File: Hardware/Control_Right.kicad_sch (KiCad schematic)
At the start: 28 parts, among them J4 BAT, J5 TagConnect, J6 1.08_MIP_MODULE, Q2 AO3401A, SW3 MSK12C02, SW4 SW_Push, U3 TPS61040DBV, U4 XIAO-NRF52840-PLUS

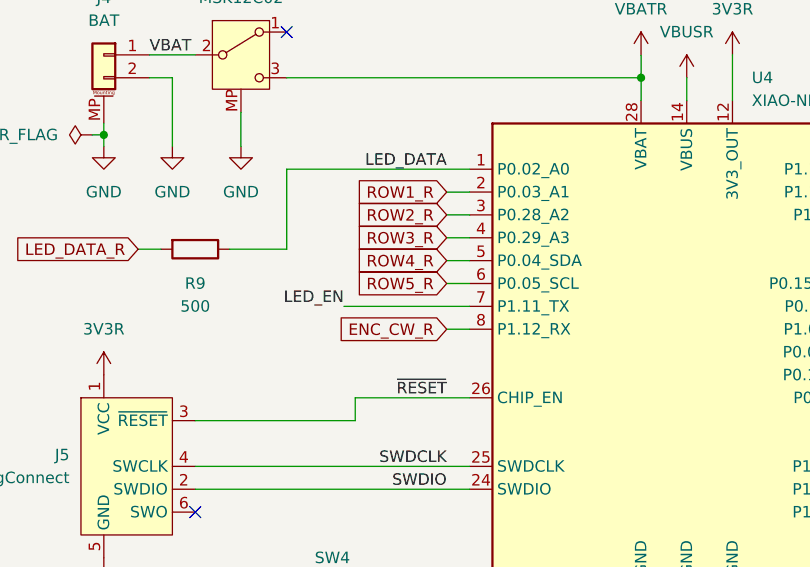
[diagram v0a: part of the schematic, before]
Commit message: Row removal and key layout
Removed the number row.
Adjusted the spacebar position and changed it to 1u.
Need to consider what to do for one of the halfs if its screen is to be removed.
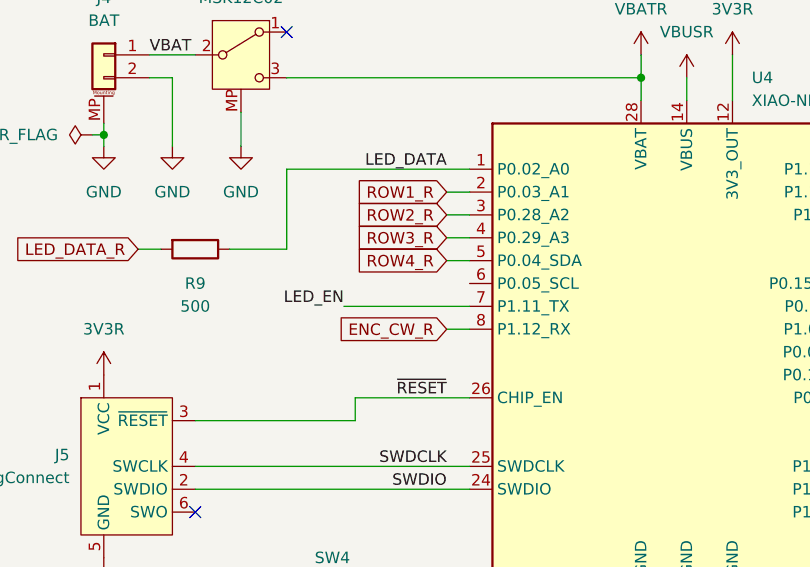
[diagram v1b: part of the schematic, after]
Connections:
- net ROW5_R: no longer names the net of U4.6 (P0.05_SCL)
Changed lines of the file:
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@@
-	(wire
-		(pts
-			(xy 87.63 66.04) (xy 90.17 66.04)
-		)
-		(stroke
-			(width 0)
-			(type default)
-		)
-	)
 	(wire
 		(pts
@@
 			)
 		)
-	)
-	(global_label "ROW5_R"
-		(shape input)
-		(at 87.63 66.04 180)
-		(fields_autoplaced yes)
-		(effects
-			(font
-				(size 1.27 1.27)
-			)
-			(justify right)
-		)
-		(property "Intersheetrefs" "${INTERSHEET_REFS}"
-			(at 77.5691 66.04 0)
-			(hide yes)
-			(show_name no)
-			(do_not_autoplace no)
-			(effects
-				(font
-					(size 1.27 1.27)
-				)
-				(justify right)
-			)
-		)

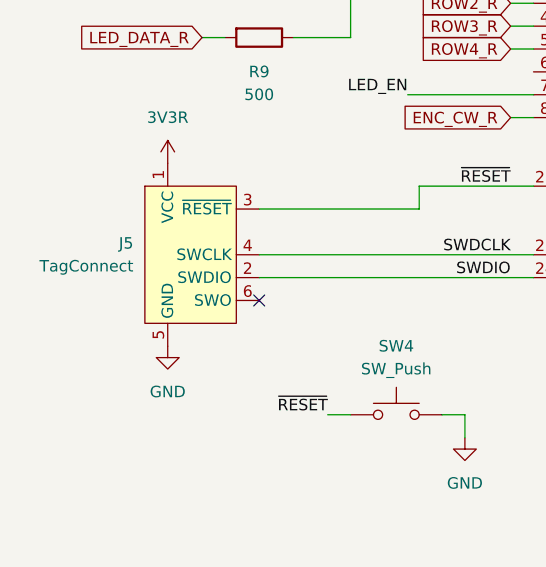
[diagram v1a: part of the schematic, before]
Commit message: Debug connector
Updated the debug connector for a custom one.
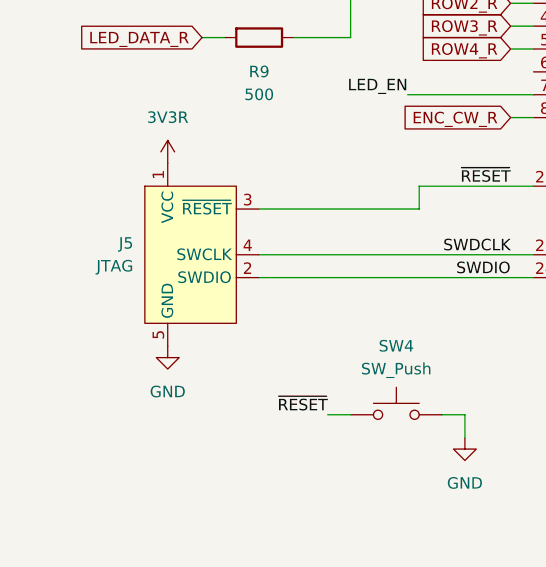
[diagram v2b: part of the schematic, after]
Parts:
- removed J5: TagConnect, Connector:Tag-Connect_TC2030-IDC-NL_2x03_P1.27mm_Vertical, symbol Connector:Conn_ARM_SWD_TagConnect_TC2030-NL
- added J5: JTAG, Custom_Parts:JTAG_SWD_1X05_1.27MM_COMBO, symbol Custom_Parts:JTAG_SWD_1X05_1.27MM_COMBO
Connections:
- net 3V3R: now also J5.1 (VCC)
- net GND: now also J5.5 (GND)
- net SWDCLK: now also J5.4 (SWCLK)
- net SWDIO: now also J5.2 (SWDIO)
- net ~{RESET}: now also J5.3 (~{RESET})
- no-connect marks 2 -> 1
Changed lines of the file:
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@@
 		(at 69.85 38.1)
 	)
-	(no_connect
-		(at 59.69 91.44)
-	)
 	(wire
 		(pts
@@
 	)
 	(symbol
-		(lib_id "Connector:Conn_ARM_SWD_TagConnect_TC2030-NL")
-		(at 52.07 86.36 0)
-		(unit 1)
-		(body_style 1)
-		(exclude_from_sim no)
-		(in_bom no)
-		(on_board yes)
-		(in_pos_files no)
-		(dnp no)
-		(fields_autoplaced yes)
-		(property "Reference" "J5"
-			(at 45.72 85.0899 0)
-			(show_name no)
-			(do_not_autoplace no)
-			(effects
-				(font
-					(size 1.27 1.27)
-				)
-				(justify right)
-			)
-		)
-		(property "Value" "TagConnect"
-			(at 45.72 87.6299 0)
-			(show_name no)
-			(do_not_autoplace no)
-			(effects
-				(font
-					(size 1.27 1.27)
-				)
-				(justify right)
-			)
-		)
-		(property "Footprint" "Connector:Tag-Connect_TC2030-IDC-NL_2x03_P1.27mm_Vertical"
-			(at 52.07 104.14 0)
-			(hide yes)
-			(show_name no)
-			(do_not_autoplace no)
-			(effects
-				(font
-					(size 1.27 1.27)
-				)
-			)
-		)
-		(property "Datasheet" "https://www.tag-connect.com/wp-content/uploads/bsk-pdf-manager/TC2030-CTX_1.pdf"
-			(at 52.07 101.6 0)
-			(hide yes)
-			(show_name no)
-			(do_not_autoplace no)
-			(effects
-				(font
-					(size 1.27 1.27)
-				)
-			)
-		)
-		(property "Description" "Tag-Connect ARM Cortex SWD JTAG connector, 6 pin, no legs"
-			(at 52.07 86.36 0)
-			(hide yes)
-			(show_name no)
-			(do_not_autoplace no)
-			(effects
-				(font
-					(size 1.27 1.27)
-				)
-			)
-		)
-		(property "JLC Part" "-"
-			(at 52.07 86.36 0)
-			(hide yes)
-			(show_name no)
-			(do_not_autoplace no)
-			(effects
-				(font
-					(size 1.27 1.27)
-				)
-			)
-		)
-		(property "Manufacturer Part" "-"
-			(at 52.07 86.36 0)
-			(hide yes)
-			(show_name no)
-			(do_not_autoplace no)
-			(effects
-				(font
-					(size 1.27 1.27)
-				)
-			)
-		)
-		(pin "2"
-		)
-		(pin "4"
-		)
-		(pin "3"
-		)
-		(pin "1"
-		)
-		(pin "5"
-		)
-		(pin "6"
-		)
-		(instances
-			(project "ValkiriaSplit"
-				(path "/7a2b6783-81dc-46bd-bbde-89342e0b1c5b/c4ce8c62-379b-42e0-bf4c-e1603684393a"
-					(reference "J5")
-					(unit 1)
-				)
-			)
-		)
-	)
-	(symbol
 		(lib_id "Custom_Parts:MSK12C02")
 		(at 64.77 40.64 0)
@@
 					(unit 1)
 				)
+			)
+		)
+	)
+	(symbol
+		(lib_id "Custom_Parts:JTAG_SWD_1X05_1.27MM_COMBO")
+		(at 52.07 86.36 0)
+		(unit 1)
+		(body_style 1)
+		(exclude_from_sim no)
+		(in_bom no)
+		(on_board yes)
+		(in_pos_files no)
+		(dnp no)
+		(fields_autoplaced yes)
+		(property "Reference" "J5"
+			(at 45.72 85.0899 0)
+			(show_name no)
+			(do_not_autoplace no)
+			(effects
+				(font
+					(size 1.27 1.27)
+				)
+				(justify right)
+			)
+		)
+		(property "Value" "JTAG"
+			(at 45.72 87.6299 0)
+			(show_name no)
+			(do_not_autoplace no)
+			(effects
+				(font
+					(size 1.27 1.27)
+				)
+				(justify right)
+			)
+		)
+		(property "Footprint" "Custom_Parts:JTAG_SWD_1X05_1.27MM_COMBO"
+			(at 52.07 104.14 0)
+			(hide yes)
+			(show_name no)
+			(do_not_autoplace no)
+			(effects
+				(font
+					(size 1.27 1.27)
+				)
+			)
+		)
+		(property "Datasheet" ""
+			(at 52.07 101.6 0)
+			(hide yes)
+			(show_name no)
+			(do_not_autoplace no)
+			(effects
+				(font
+					(size 1.27 1.27)
+				)
+			)
+		)
+		(property "Description" "Custom JTAG connector based on 1x05 pad footprint"
+			(at 52.07 86.36 0)
+			(hide yes)
+			(show_name no)
+			(do_not_autoplace no)
+			(effects
+				(font
+					(size 1.27 1.27)
+				)
+			)
+		)
+		(property "JLC Part" "-"
+			(at 52.07 86.36 0)
+			(hide yes)
+			(show_name no)
+			(do_not_autoplace no)
+			(effects
+				(font
+					(size 1.27 1.27)
+				)
+			)
+		)
+		(property "Manufacturer Part" "-"
+			(at 52.07 86.36 0)
+			(hide yes)
+			(show_name no)
+			(do_not_autoplace no)
+			(effects
+				(font
+					(size 1.27 1.27)
+				)
+			)
+		)
+		(pin "5"
+		)
+		(pin "2"
+		)
+		(pin "3"
+		)
+		(pin "4"
+		)
+		(pin "1"
+		)
+		(instances
+			(project "ValkiriaSplit"
+				(path "/7a2b6783-81dc-46bd-bbde-89342e0b1c5b/c4ce8c62-379b-42e0-bf4c-e1603684393a"
+					(reference "J5")
+					(unit 1)
+				)

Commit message: Board outline and routing
Enlarged the board outline by 0.5mm for proper fitment of the switch receptacles.
Updated the footprint for the switch receptacles.
Changed the JTAG connector for a custom one.
Need to review the size of the PCB area dedicated to the MCU and the screen.
Need to consider removing the additional reset button.
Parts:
- D3, D4: value DSK24 -> DSL14; JLC Part C22466352 -> C22466349; Manufacturer Part DSK24 -> DSL14
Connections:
- net SWDCLK: now also J5.2 (SWCLK); no longer J5.4 (SWCLK)
- net SWDIO: now also J5.3 (SWDIO); no longer J5.2 (SWDIO)
- net ~{RESET}: now also J5.4 (~{RESET}); no longer J5.3 (~{RESET})
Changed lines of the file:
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@@
 			)
 		)
-		(property "Value" "DSK24"
+		(property "Value" "DSL14"
 			(at 122.2375 143.51 0)
 			(show_name no)
@@
 			)
 		)
-		(property "JLC Part" "C22466352"
+		(property "JLC Part" "C22466349"
 			(at 121.92 147.32 0)
 			(hide yes)
@@
 			)
 		)
-		(property "Manufacturer Part" "DSK24"
+		(property "Manufacturer Part" "DSL14"
 			(at 121.92 147.32 0)
 			(hide yes)
@@
 			)
 		)
-		(property "Value" "DSK24"
+		(property "Value" "DSL14"
 			(at 68.8975 153.67 0)
 			(show_name no)
@@
 			)
 		)
-		(property "JLC Part" "C22466352"
+		(property "JLC Part" "C22466349"
 			(at 68.58 157.48 0)
 			(hide yes)
@@
 			)
 		)
-		(property "Manufacturer Part" "DSK24"
+		(property "Manufacturer Part" "DSL14"
 			(at 68.58 157.48 0)
 			(hide yes)
@@
 		(pin "2"
 		)
-		(pin "3"
-		)
 		(pin "4"
 		)
+		(pin "3"
+		)
 		(pin "1"

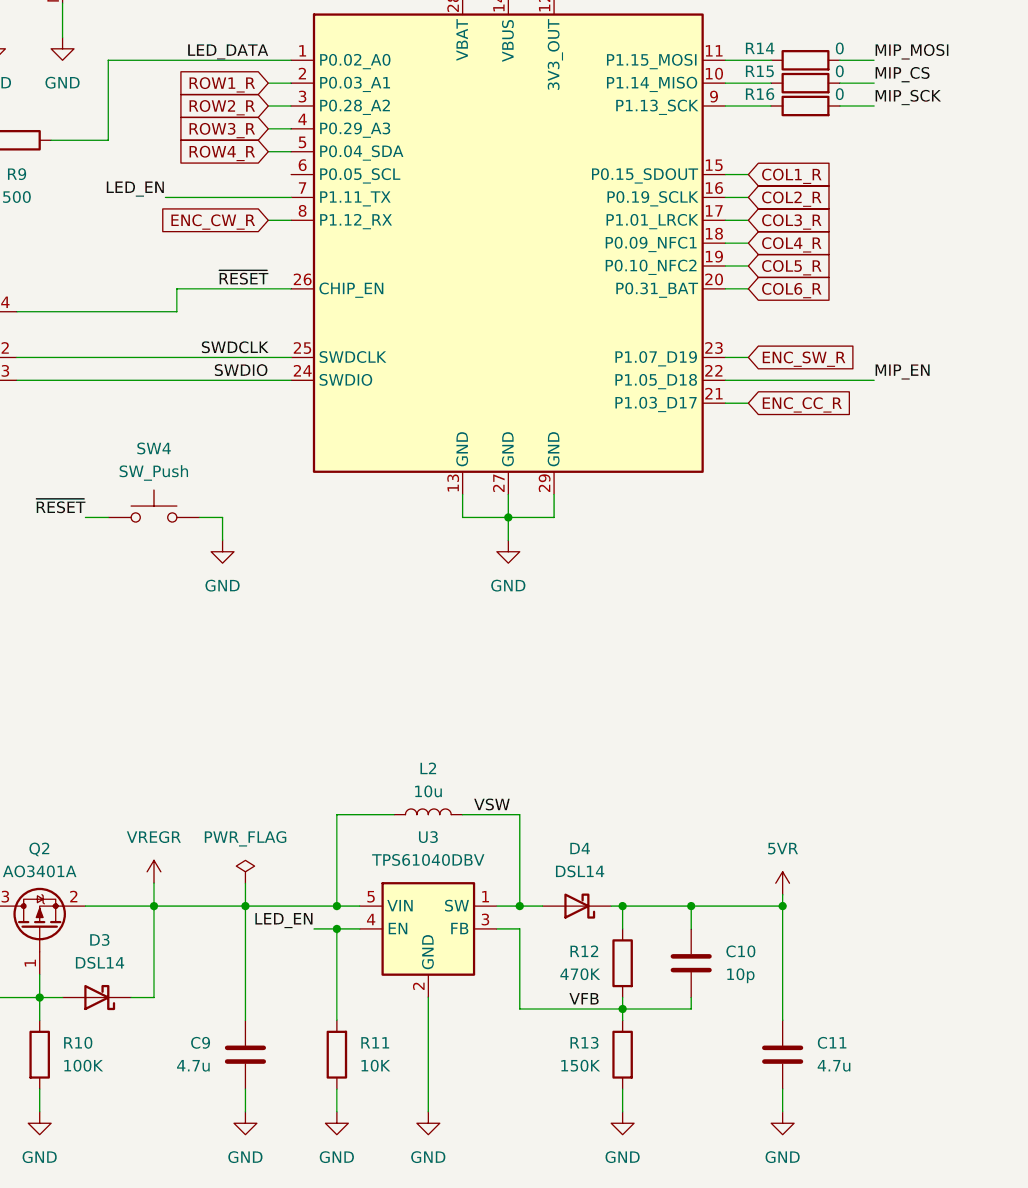
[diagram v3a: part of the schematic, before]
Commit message: Display model and layout
Updated the 3D model and footprint for the MIP display. It now sits further from the PCB.
Continued the layout and routing of the left side PCB.
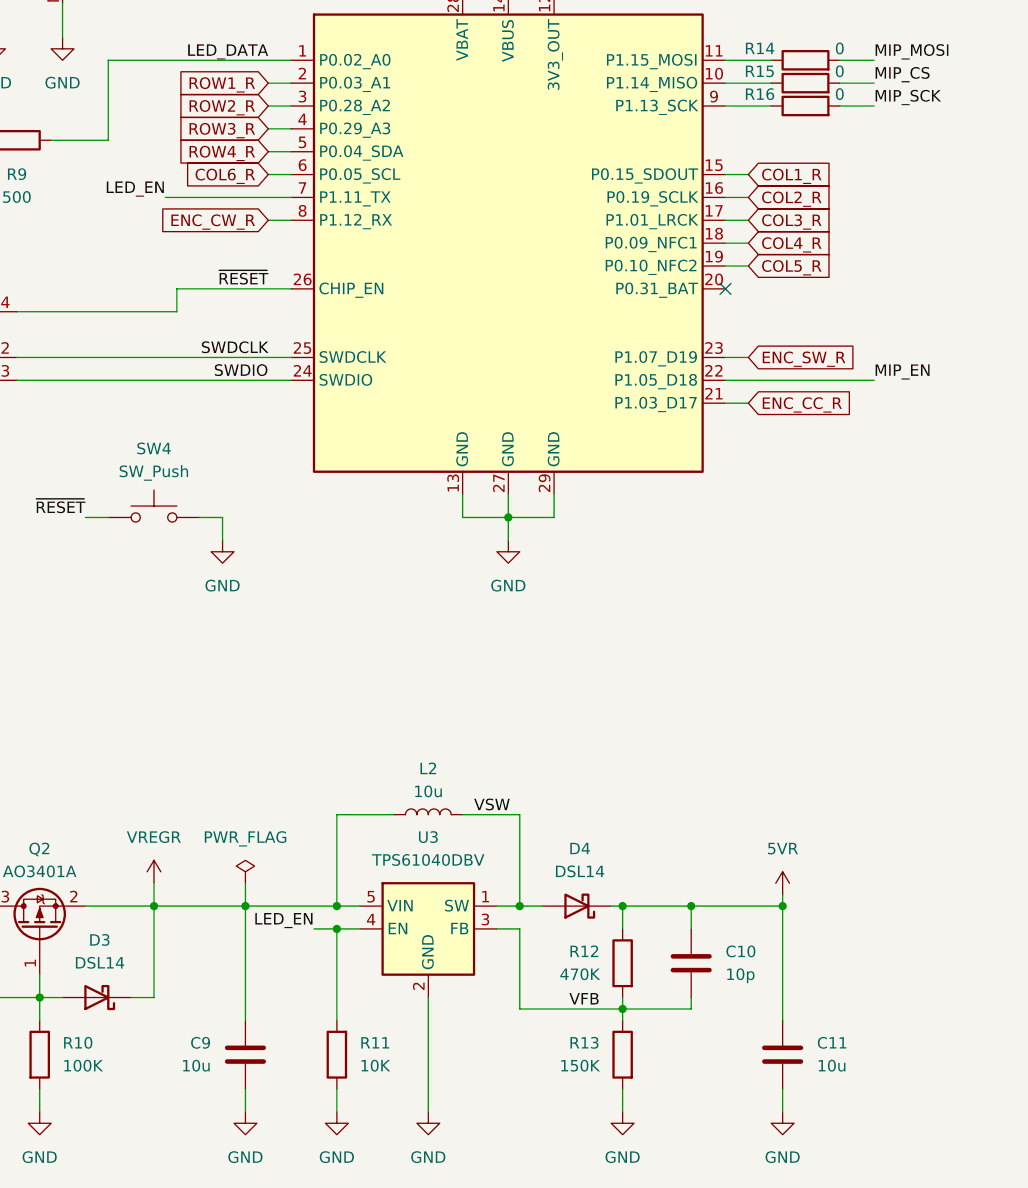
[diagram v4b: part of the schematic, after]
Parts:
- C11, C9: value 4.7u -> 10u; footprint Capacitor_SMD:C_1206_3216Metric -> Capacitor_SMD:C_0603_1608Metric; JLC Part C29823 -> C96446; Manufacturer Part 1206B475K500NT -> CL10A106MA8NRNC
- J6: footprint Custom_Parts:1.08_MIP_MODULE -> Custom_Parts:1.08_MIP_MODULE_TALL
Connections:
- net COL6_R: now also U4.6 (P0.05_SCL); no longer U4.20 (P0.31_BAT)
- no-connect marks 1 -> 2
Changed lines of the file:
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@@
 		(at 69.85 38.1)
 	)
+	(no_connect
+		(at 138.43 78.74)
+	)
 	(wire
 		(pts
@@
 	(wire
 		(pts
-			(xy 138.43 78.74) (xy 140.97 78.74)
-		)
-		(stroke
-			(width 0)
-			(type default)
-		)
-	)
-	(wire
-		(pts
 			(xy 87.63 60.96) (xy 90.17 60.96)
 		)
@@
 	(wire
 		(pts
+			(xy 87.63 66.04) (xy 90.17 66.04)
+		)
+		(stroke
+			(width 0)
+			(type default)
+		)
+	)
+	(wire
+		(pts
 			(xy 193.04 106.68) (xy 193.04 121.92)
 		)
@@
 	(global_label "COL6_R"
 		(shape input)
-		(at 140.97 78.74 0)
+		(at 87.63 66.04 180)
 		(fields_autoplaced yes)
 		(effects
@@
 				(size 1.27 1.27)
 			)
-			(justify left)
+			(justify right)
 		)
 		(property "Intersheetrefs" "${INTERSHEET_REFS}"
-			(at 153.4499 78.74 0)
+			(at 77.5691 66.04 0)
 			(hide yes)
 			(show_name no)
@@
 					(size 1.27 1.27)
 				)
-				(justify left)
+				(justify right)
 			)
 		)
@@
 			)
 		)
-		(property "Value" "4.7u"
+		(property "Value" "10u"
 			(at 148.59 165.0999 0)
 			(show_name no)
@@
 			)
 		)
-		(property "Footprint" "Capacitor_SMD:C_1206_3216Metric"
+		(property "Footprint" "Capacitor_SMD:C_0603_1608Metric"
 			(at 145.7452 167.64 0)
 			(hide yes)
@@
 			)
 		)
-		(property "JLC Part" "C29823"
+		(property "JLC Part" "C96446"
 			(at 144.78 163.83 0)
 			(hide yes)
@@
 			)
 		)
-		(property "Manufacturer Part" "1206B475K500NT"
+		(property "Manufacturer Part" "CL10A106MA8NRNC"
 			(at 144.78 163.83 0)
 			(hide yes)
@@
 			)
 		)
-		(property "Footprint" "Custom_Parts:1.08_MIP_MODULE"
+		(property "Footprint" "Custom_Parts:1.08_MIP_MODULE_TALL"
 			(at 238.76 120.65 0)
 			(hide yes)
@@
 			)
 		)
-		(property "Value" "4.7u"
+		(property "Value" "10u"
 			(at 81.28 165.0999 0)
 			(show_name no)
@@
 			)
 		)
-		(property "Footprint" "Capacitor_SMD:C_1206_3216Metric"
+		(property "Footprint" "Capacitor_SMD:C_0603_1608Metric"
 			(at 84.1248 167.64 0)
 			(hide yes)
@@
 			)
 		)
-		(property "JLC Part" "C29823"
+		(property "JLC Part" "C96446"
 			(at 85.09 163.83 0)
 			(hide yes)
@@
 			)
 		)
-		(property "Manufacturer Part" "1206B475K500NT"
+		(property "Manufacturer Part" "CL10A106MA8NRNC"
 			(at 85.09 163.83 0)
 			(hide yes)

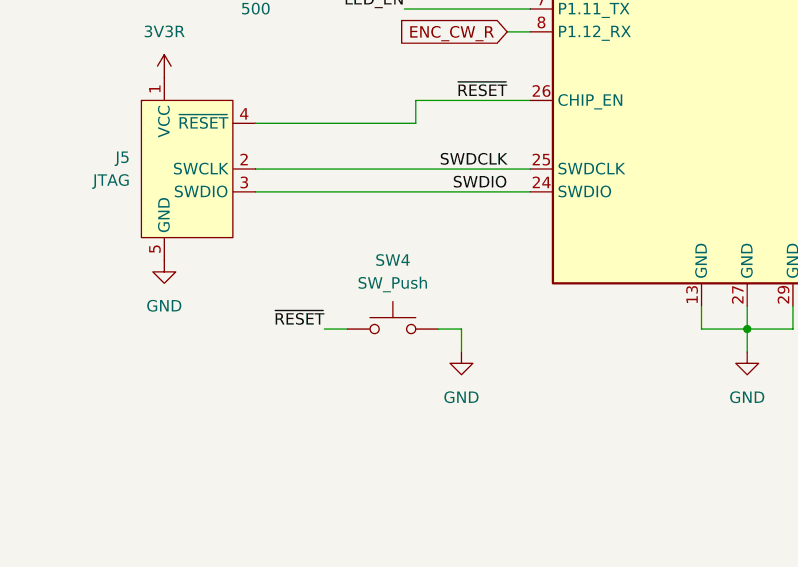
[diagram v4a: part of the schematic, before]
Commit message: Matrix routing and data lines
Routed some of the lines for the switch matrix.
Routed the singal lines for the MIP display.
Need to check clearenaces and spacing between the SPI lines.
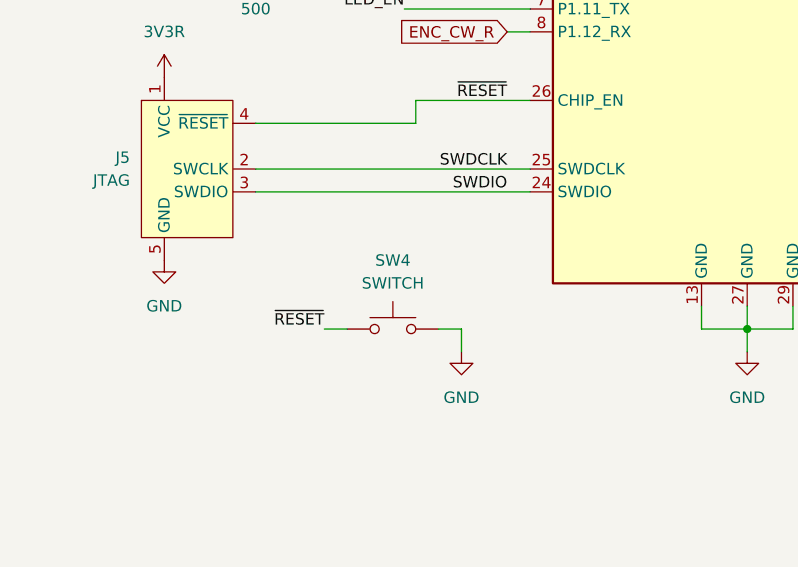
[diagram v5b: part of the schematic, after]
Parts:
- J4: footprint Custom_Parts:JST_PH_1x02_P2.00MM_SMD_HOR -> Custom_Parts:JST_ZH_1x02_P1.50MM_SMD_HORIZONTAL; JLC Part C3029440 -> C722913; Manufacturer Part WAFER-PH2.0-2PWB -> ZH1.5-2P-WT
- SW4: value SW_Push -> SWITCH
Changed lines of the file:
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@@
 			)
 		)
-		(property "Footprint" "Custom_Parts:JST_PH_1x02_P2.00MM_SMD_HOR"
+		(property "Footprint" "Custom_Parts:JST_ZH_1x02_P1.50MM_SMD_HORIZONTAL"
 			(at 49.53 40.64 0)
 			(hide yes)
@@
 			)
 		)
-		(property "JLC Part" "C3029440"
+		(property "JLC Part" "C722913"
 			(at 49.53 40.64 0)
 			(hide yes)
@@
 			)
 		)
-		(property "Manufacturer Part" "WAFER-PH2.0-2PWB"
+		(property "Manufacturer Part" "ZH1.5-2P-WT"
 			(at 49.53 40.64 0)
 			(hide yes)
@@
 			)
 		)
-		(property "Value" "SW_Push"
+		(property "Value" "SWITCH"
 			(at 74.93 99.06 0)
 			(show_name no)
